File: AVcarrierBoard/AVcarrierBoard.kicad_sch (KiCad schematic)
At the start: 16 parts, among them J1 MainRecov, J3 DrogRecov, J4 Mech_Switch, J5 Mech_Switch, J6 462070006, U1 EggfinderMini/FeatherGPS, U2 EggtimerQuark, U3 Blue_Raven, U4 WiFi Switch, U5 WiFi Switch

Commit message: editedd
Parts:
- H1, H2, H3, H4: footprint (none) -> MountingHole:MountingHole_3.2mm_M3_ISO14580
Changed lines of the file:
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@@
       (effects (font (size 1.27 1.27)) (justify left))
     )
-    (property "Footprint" "" (at 134.62 134.62 0)
+    (property "Footprint" "MountingHole:MountingHole_3.2mm_M3_ISO14580" (at 134.62 134.62 0)
       (effects (font (size 1.27 1.27)) hide)
     )
@@
       (effects (font (size 1.27 1.27)) (justify left))
     )
-    (property "Footprint" "" (at 179.07 134.62 0)
+    (property "Footprint" "MountingHole:MountingHole_3.2mm_M3_ISO14580" (at 179.07 134.62 0)
       (effects (font (size 1.27 1.27)) hide)
     )
@@
       (effects (font (size 1.27 1.27)) (justify left))
     )
-    (property "Footprint" "" (at 149.86 134.62 0)
+    (property "Footprint" "MountingHole:MountingHole_3.2mm_M3_ISO14580" (at 149.86 134.62 0)
       (effects (font (size 1.27 1.27)) hide)
     )
@@
       (effects (font (size 1.27 1.27)) (justify left))
     )
-    (property "Footprint" "" (at 163.83 134.62 0)
-      (effects (font (size 1.27 1.27)) hide)
-    )
+    (property "Footprint" "MountingHole:MountingHole_3.2mm_M3_ISO14580" (at 163.83 134.62 0)
+      (effects (font (size 1.27 1.27)) hide)
+    )

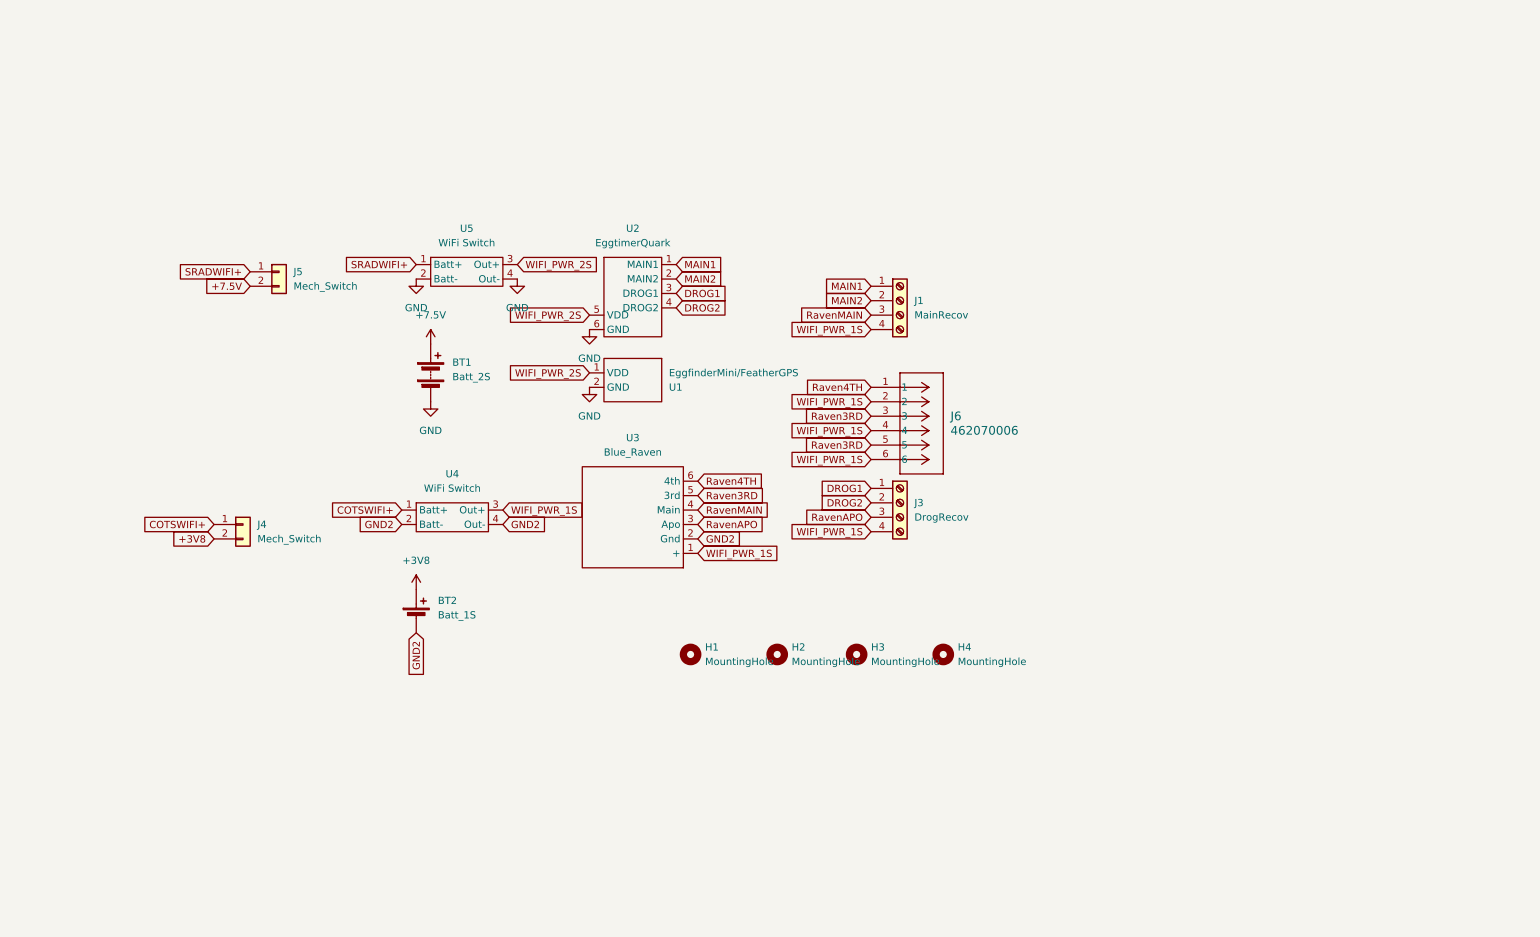
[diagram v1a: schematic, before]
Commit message: Schematic updated based on Ethan's review
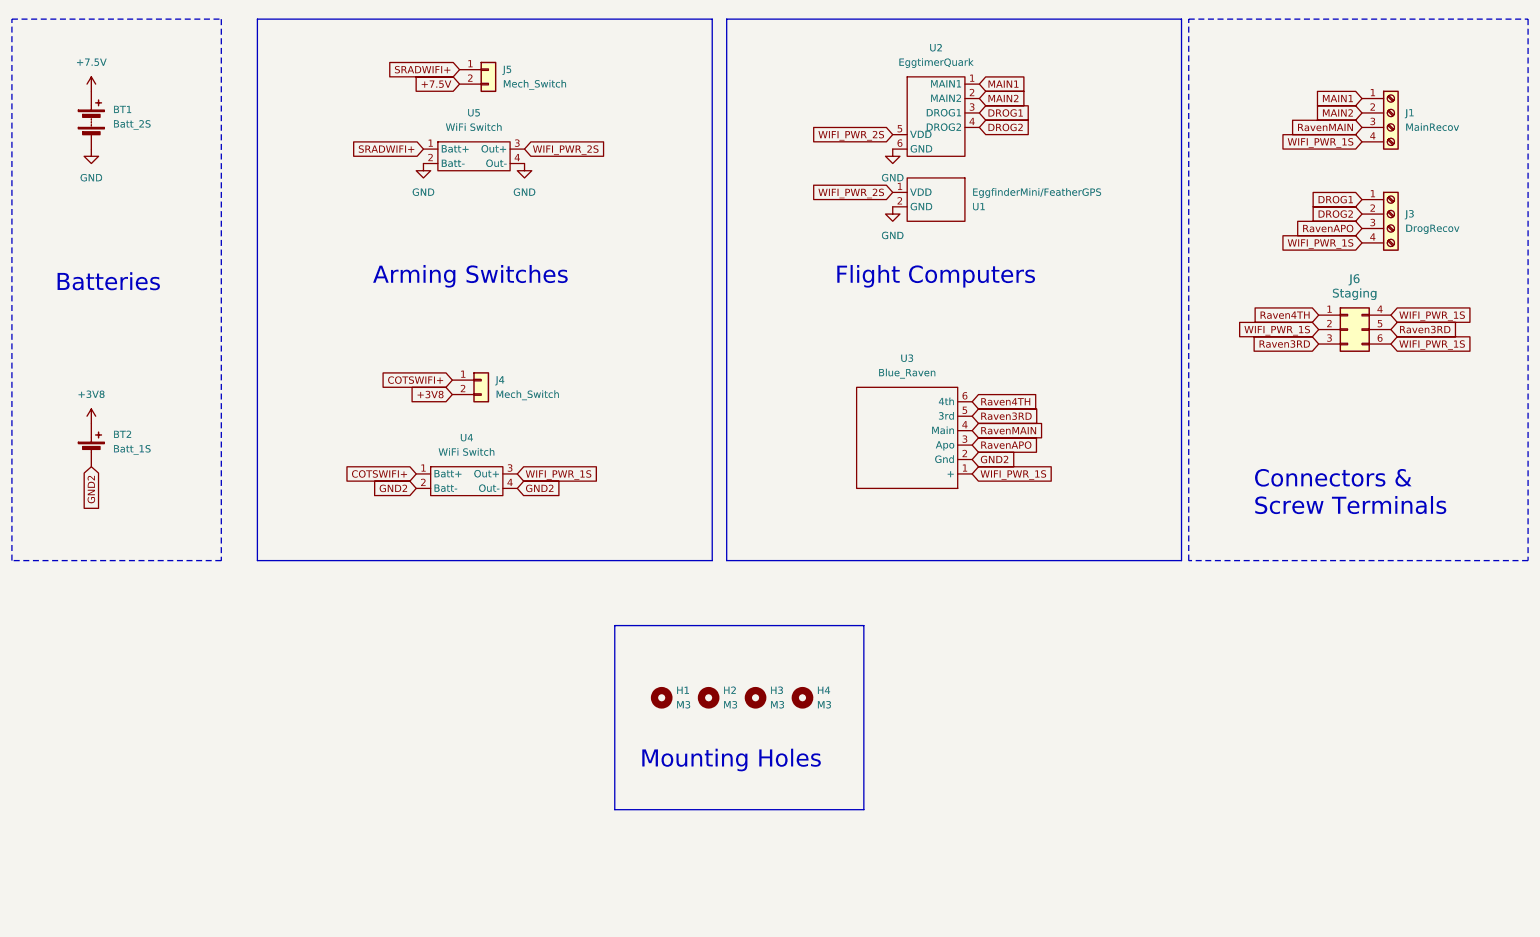
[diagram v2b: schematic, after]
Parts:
- H1, H2, H3, H4: value MountingHole -> M3
- J6: value 462070006 -> Staging; symbol COTS_boards:462070006 -> Connector_Generic:Conn_02x03_Top_Bottom
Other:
- note added: "Arming Switches"
- note added: "Batteries"
- note added: "Connectors & Screw Terminals"
- note added: "Flight Computers"
- note added: "Mounting Holes"
- moved on the sheet: BT1, BT2, H1, H2, H3, H4, J1, J3, J4, J5, U1, U2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

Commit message: Added additional igniter switch, replaced quark with quantum, and updated PCB
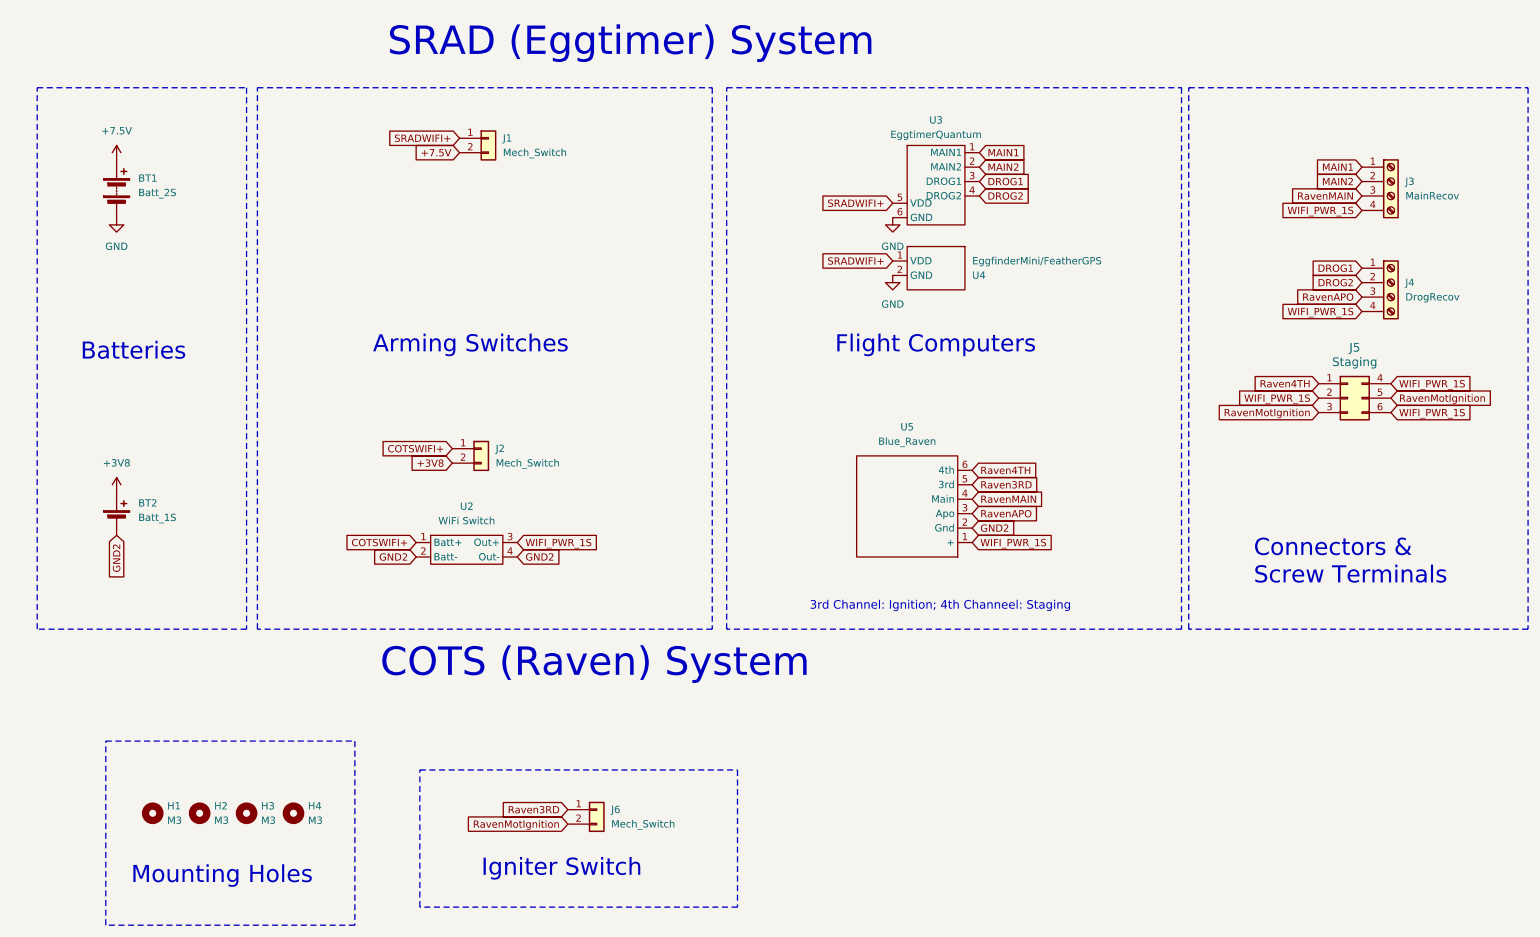
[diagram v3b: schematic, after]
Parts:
- removed U5: WiFi Switch, COTS_Boards:Eggtime_WiFi_switch, symbol COTS_boards:Eggtimer_WiFi_switch
- added J6: Mech_Switch, Connector_PinHeader_2.54mm:PinHeader_1x02_P2.54mm_Vertical, symbol Connector_Generic:Conn_01x02
- U3: renamed from U2; value EggtimerQuark -> EggtimerQuantum; footprint COTS_Boards:EggtimerQuark -> COTS_Boards:EggtimerQuantum; symbol COTS_boards:EggtimerQuark -> COTS_boards:EggtimerQuantum
- renumbered J5 to J1, J4 to J2, J1 to J3, J3 to J4, J6 to J5, U4 to U2, U1 to U4, U3 to U5
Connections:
- net WIFI_PWR_2S is gone; now on net SRADWIFI+: U3.5 (VDD), U4.1 (VDD)
- net Raven3RD: now also J6.1 (Pin_1); no longer J5.3 (Pin_3), J5.5 (Pin_5)
- new net RavenMotIgnition: J5.3 (Pin_3), J5.5 (Pin_5), J6.2 (Pin_2)
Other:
- note added: "3rd Channel: Ignition; 4th Channeel: Staging"
- note added: "COTS (Raven) System"
- note added: "Igniter Switch"
- note added: "SRAD (Eggtimer) System"
- moved on the sheet: BT1, BT2, H1, H2, H3, H4, J1, J2, J3, J4, J5, U2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

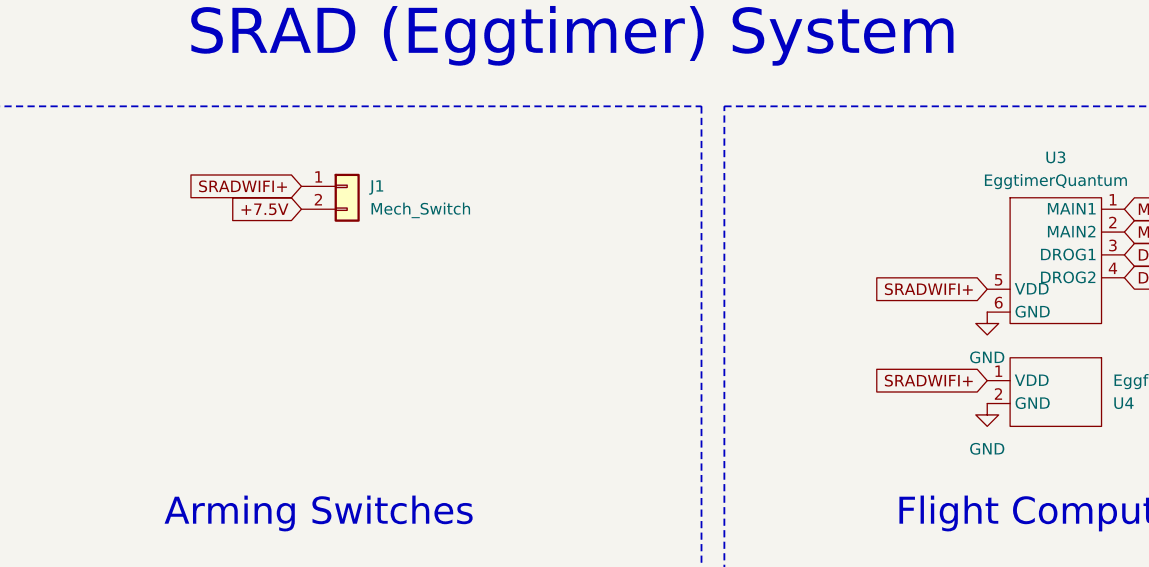
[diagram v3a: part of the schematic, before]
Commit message: Updated PCB, made new nets and vias according to last change. Did not fill power layers yet.
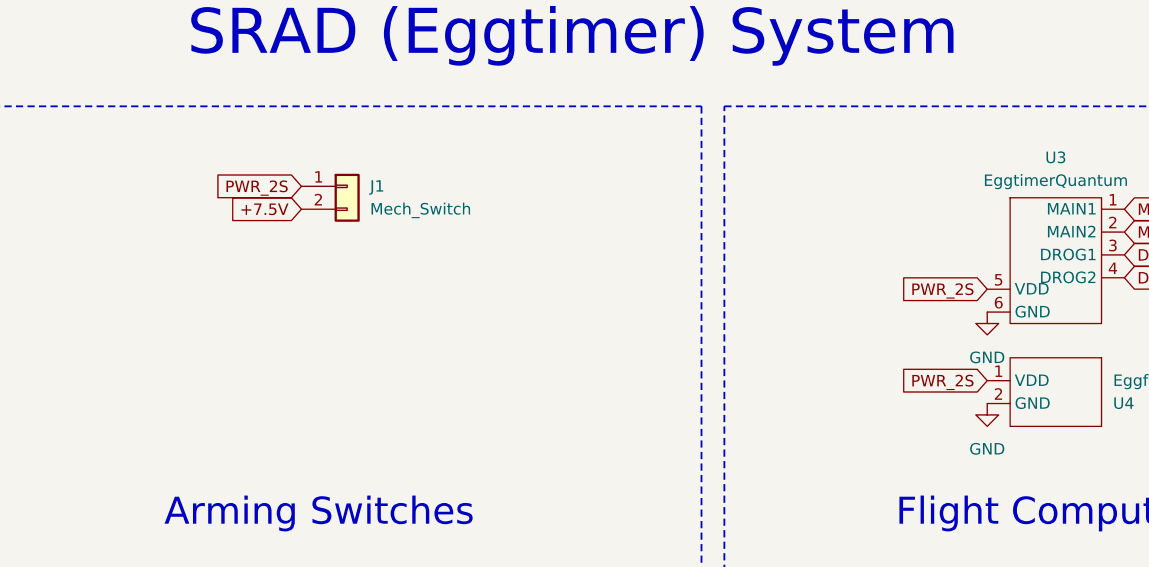
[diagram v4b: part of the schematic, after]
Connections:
- net SRADWIFI+ renamed PWR_2S
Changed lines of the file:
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@@
-    )
-  )
-  (global_label "SRADWIFI+" (shape input) (at 170.18 65.405 180) (fields_autoplaced)
-    (effects (font (size 1.27 1.27)) (justify right))
-    (property "Intersheetrefs" "${INTERSHEET_REFS}" (at 157.0347 65.405 0)
-      (effects (font (size 1.27 1.27)) (justify right) hide)
     )
   )
@@
     (property "Intersheetrefs" "${INTERSHEET_REFS}" (at 196.4485 109.855 0)
       (effects (font (size 1.27 1.27)) (justify left) hide)
+    )
+  )
+  (global_label "PWR_2S" (shape input) (at 170.18 55.245 180) (fields_autoplaced)
+    (effects (font (size 1.27 1.27)) (justify right))
+    (property "Intersheetrefs" "${INTERSHEET_REFS}" (at 159.8168 55.245 0)
+      (effects (font (size 1.27 1.27)) (justify right) hide)
     )
   )
@@
     (effects (font (size 1.27 1.27)) (justify right))
     (property "Intersheetrefs" "${INTERSHEET_REFS}" (at 230.0296 89.535 0)
-      (effects (font (size 1.27 1.27)) (justify right) hide)
-    )
-  )
-  (global_label "SRADWIFI+" (shape input) (at 170.18 55.245 180) (fields_autoplaced)
-    (effects (font (size 1.27 1.27)) (justify right))
-    (property "Intersheetrefs" "${INTERSHEET_REFS}" (at 157.0347 55.245 0)
       (effects (font (size 1.27 1.27)) (justify right) hide)
     )
@@
     )
   )
-  (global_label "SRADWIFI+" (shape input) (at 93.98 43.815 180) (fields_autoplaced)
+  (global_label "PWR_2S" (shape input) (at 93.98 43.815 180) (fields_autoplaced)
     (effects (font (size 1.27 1.27)) (justify right))
-    (property "Intersheetrefs" "${INTERSHEET_REFS}" (at 80.8347 43.815 0)
+    (property "Intersheetrefs" "${INTERSHEET_REFS}" (at 83.6168 43.815 0)
       (effects (font (size 1.27 1.27)) (justify right) hide)
     )
+  )
+  (global_label "PWR_2S" (shape input) (at 170.18 65.405 180) (fields_autoplaced)
+    (effects (font (size 1.27 1.27)) (justify right))
+    (property "Intersheetrefs" "${INTERSHEET_REFS}" (at 159.8168 65.405 0)
+      (effects (font (size 1.27 1.27)) (justify right) hide)
+    )

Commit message: More PCB changes according to Ethan's review
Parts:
- J1, J2: footprint Connector_PinHeader_2.54mm:PinHeader_1x02_P2.54mm_Vertical -> Connector_PinHeader_2.54mm:PinHeader_1x02_P2.97mm_Vertical
- J3: footprint COTS_Boards:TE_282837-4 -> COTS_Boards:TE_282837-4-2
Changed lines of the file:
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@@
       (effects (font (size 1.27 1.27)) (justify left))
     )
-    (property "Footprint" "COTS_Boards:TE_282837-4" (at 257.81 51.435 0)
+    (property "Footprint" "COTS_Boards:TE_282837-4-2" (at 257.81 51.435 0)
       (effects (font (size 1.27 1.27)) hide)
     )
@@
       (effects (font (size 1.27 1.27)) (justify left))
     )
-    (property "Footprint" "Connector_PinHeader_2.54mm:PinHeader_1x02_P2.54mm_Vertical" (at 99.06 43.815 0)
+    (property "Footprint" "Connector_PinHeader_2.54mm:PinHeader_1x02_P2.97mm_Vertical" (at 99.06 43.815 0)
       (effects (font (size 1.27 1.27)) hide)
     )
@@
       (effects (font (size 1.27 1.27)) (justify left))
     )
-    (property "Footprint" "Connector_PinHeader_2.54mm:PinHeader_1x02_P2.54mm_Vertical" (at 97.79 98.425 0)
+    (property "Footprint" "Connector_PinHeader_2.54mm:PinHeader_1x02_P2.97mm_Vertical" (at 97.79 98.425 0)
       (effects (font (size 1.27 1.27)) hide)
     )

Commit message: Rerouted footprint directory
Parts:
- J1, J2: footprint Connector_PinHeader_2.54mm:PinHeader_1x02_P2.97mm_Vertical -> 2.97mmConnector:PinHeader_1x02_P2.97mm_Vertical
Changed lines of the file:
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@@
       (effects (font (size 1.27 1.27)) (justify left))
     )
-    (property "Footprint" "Connector_PinHeader_2.54mm:PinHeader_1x02_P2.97mm_Vertical" (at 99.06 43.815 0)
+    (property "Footprint" "2.97mmConnector:PinHeader_1x02_P2.97mm_Vertical" (at 99.06 43.815 0)
       (effects (font (size 1.27 1.27)) hide)
     )
@@
       (effects (font (size 1.27 1.27)) (justify left))
     )
-    (property "Footprint" "Connector_PinHeader_2.54mm:PinHeader_1x02_P2.97mm_Vertical" (at 97.79 98.425 0)
+    (property "Footprint" "2.97mmConnector:PinHeader_1x02_P2.97mm_Vertical" (at 97.79 98.425 0)
       (effects (font (size 1.27 1.27)) hide)
     )
